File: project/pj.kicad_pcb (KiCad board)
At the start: 2 copper layers, 65 x 56.5 mm, 18 parts, among them J1 RPi_GPIO, J10 Pico PWR enable, J2 2B+, J3 zero, J4 3A+, J5 3B+, J6 4, J7 Conn_01x02, J8 Conn_01x02, J9 External PWR, SW1 SW_Push, SW2 SW_Push

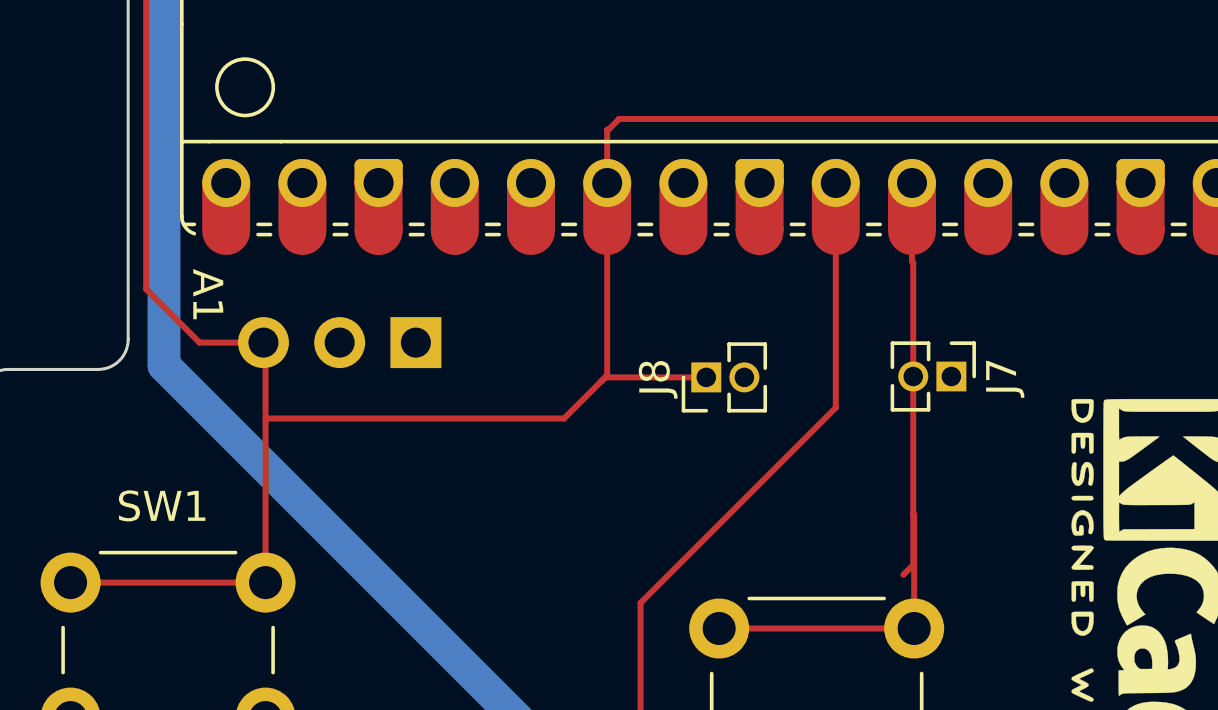
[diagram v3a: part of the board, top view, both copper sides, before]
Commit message: move holes to make room for more holes
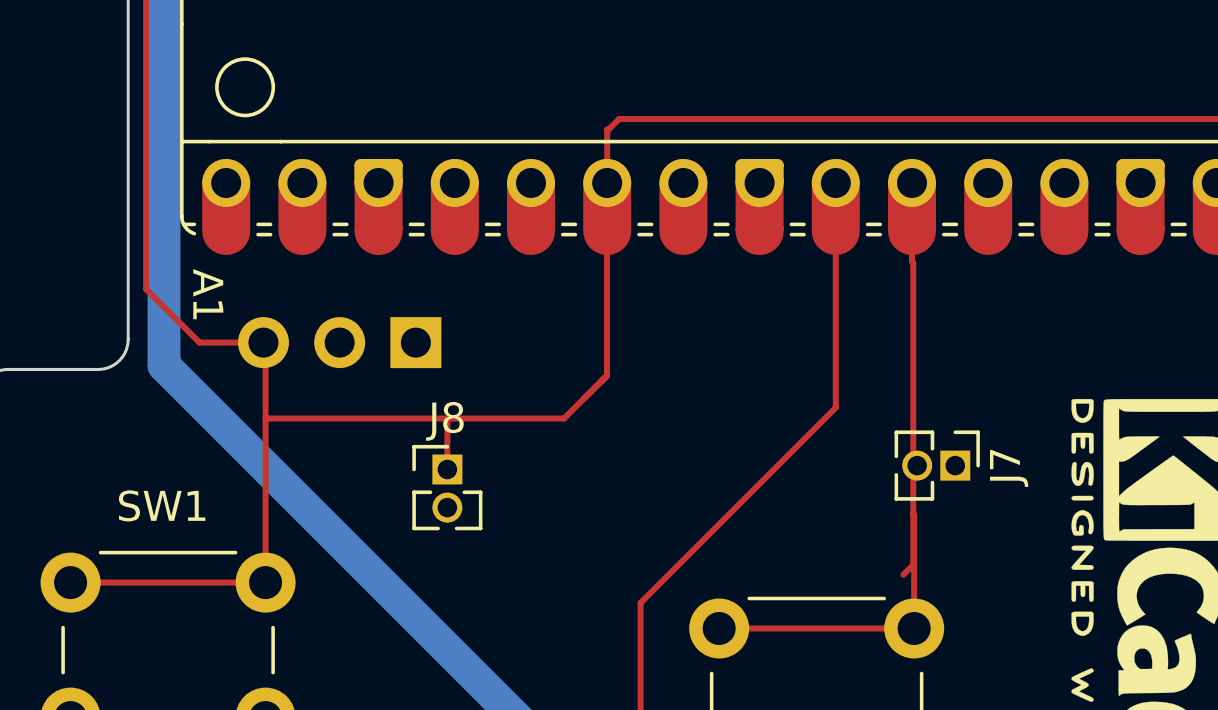
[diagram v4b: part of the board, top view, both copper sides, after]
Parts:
- moved J8 9.16 mm to (52.1, 80.8), turned to 0 degrees
- moved J7 2.97 mm to (69.0, 80.7)
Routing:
- net Net-(A1-GPIO20): track 136.3 -> 135.7 mm
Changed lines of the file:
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@@
 	(footprint "Connector_PinHeader_1.27mm:PinHeader_1x02_P1.27mm_Vertical"
 		(layer "F.Cu")
-		(at 60.69 77.76 90)
+		(at 52.06 80.83)
 		(descr "Through hole straight pin header, 1x02, 1.27mm pitch, single row")
 		(tags "Through hole pin header THT 1x02 1.27mm single row")
 		(property "Reference" "J8"
-			(at 0 -1.695 90)
+			(at 0 -1.695 360)
 			(layer "F.SilkS")
 			(effects
@@
 		)
 		(property "Value" "Conn_01x02"
-			(at 0 2.965 90)
+			(at 0 2.965 360)
 			(layer "F.Fab")
 			(effects
@@
 		)
 		(property "Footprint" "Connector_PinHeader_1.27mm:PinHeader_1x02_P1.27mm_Vertical"
-			(at 0 0 90)
+			(at 0 0 0)
 			(unlocked yes)
 			(layer "F.Fab")
@@
 		)
 		(property "Datasheet" ""
-			(at 0 0 90)
+			(at 0 0 0)
 			(unlocked yes)
 			(layer "F.Fab")
@@
 		)
 		(property "Description" "Generic connector, single row, 01x02, script generated (kicad-library-utils/schlib/autogen/connector/)"
-			(at 0 0 90)
+			(at 0 0 0)
 			(unlocked yes)
 			(layer "F.Fab")
@@
 		)
 		(fp_line
-			(start 1.11 0.76)
-			(end 1.11 1.965)
+			(start -1.11 0.76)
+			(end -1.11 1.965)
 			(stroke
 				(width 0.12)
@@
 		)
 		(fp_line
-			(start 0.563471 0.76)
-			(end 1.11 0.76)
+			(start -1.11 0.76)
+			(end -0.563471 0.76)
 			(stroke
 				(width 0.12)
@@
 		)
 		(fp_line
-			(start -1.11 0.76)
-			(end -0.563471 0.76)
+			(start -1.11 1.965)
+			(end -0.30753 1.965)
 			(stroke
 				(width 0.12)
@@
 		)
 		(fp_line
-			(start -1.11 0.76)
-			(end -1.11 1.965)
+			(start 0.30753 1.965)
+			(end 1.11 1.965)
 			(stroke
 				(width 0.12)
@@
 		)
 		(fp_line
-			(start 0.30753 1.965)
-			(end 1.11 1.965)
+			(start 0.563471 0.76)
+			(end 1.11 0.76)
 			(stroke
 				(width 0.12)
@@
 		)
 		(fp_line
-			(start -1.11 1.965)
-			(end -0.30753 1.965)
+			(start 1.11 0.76)
+			(end 1.11 1.965)
 			(stroke
 				(width 0.12)
@@
 		)
 		(fp_line
-			(start 1.55 -1.15)
-			(end -1.55 -1.15)
+			(start -1.55 -1.15)
+			(end -1.55 2.45)
 			(stroke
 				(width 0.05)
@@
 		)
 		(fp_line
-			(start -1.55 -1.15)
-			(end -1.55 2.45)
+			(start -1.55 2.45)
+			(end 1.55 2.45)
 			(stroke
 				(width 0.05)
@@
 		)
 		(fp_line
-			(start 1.55 2.45)
-			(end 1.55 -1.15)
+			(start 1.55 -1.15)
+			(end -1.55 -1.15)
 			(stroke
 				(width 0.05)
@@
 		)
 		(fp_line
-			(start -1.55 2.45)
-			(end 1.55 2.45)
+			(start 1.55 2.45)
+			(end 1.55 -1.15)
 			(stroke
 				(width 0.05)
@@
 		)
 		(fp_line
-			(start 1.05 -0.635)
-			(end 1.05 1.905)
+			(start -1.05 -0.11)
+			(end -0.525 -0.635)
 			(stroke
 				(width 0.1)
@@
 		)
 		(fp_line
-			(start -0.525 -0.635)
-			(end 1.05 -0.635)
+			(start -1.05 1.905)
+			(end -1.05 -0.11)
 			(stroke
 				(width 0.1)
@@
 		)
 		(fp_line
-			(start -1.05 -0.11)
-			(end -0.525 -0.635)
+			(start -0.525 -0.635)
+			(end 1.05 -0.635)
 			(stroke
 				(width 0.1)
@@
 		)
 		(fp_line
-			(start 1.05 1.905)
-			(end -1.05 1.905)
+			(start 1.05 -0.635)
+			(end 1.05 1.905)
 			(stroke
 				(width 0.1)
@@
 		)
 		(fp_line
-			(start -1.05 1.905)
-			(end -1.05 -0.11)
+			(start 1.05 1.905)
+			(end -1.05 1.905)
 			(stroke
 				(width 0.1)
@@
 		)
 		(fp_text user "${REFERENCE}"
-			(at 0 0.635 0)
+			(at 0 0.635 90)
 			(layer "F.Fab")
 			(effects
@@
 		)
 		(pad "1" thru_hole rect
-			(at 0 0 90)
+			(at 0 0)
 			(size 1 1)
 			(drill 0.65)
@@
 		)
 		(pad "2" thru_hole oval
-			(at 0 1.27 90)
+			(at 0 1.27)
 			(size 1 1)
 			(drill 0.65)
@@
 		(fp_arc
 			(start 10.579676 25.189937)
-			(mid 10.35796 25.493961)
+			(mid 10.357949 25.493953)
 			(end 10 25.61)
 			(stroke
@@
 	(footprint "Connector_PinHeader_1.27mm:PinHeader_1x02_P1.27mm_Vertical"
 		(layer "F.Cu")
-		(at 68.86 77.73 -90)
+		(at 68.99 80.7 -90)
 		(descr "Through hole straight pin header, 1x02, 1.27mm pitch, single row")
 		(tags "Through hole pin header THT 1x02 1.27mm single row")
@@
 	)
 	(segment
+		(start 55.95 79.13)
+		(end 56.615 78.465)
+		(width 0.2)
+		(layer "F.Cu")
+		(net 9)
+	)
+	(segment
 		(start 44.82 48.37)
 		(end 40.61 48.37)
@@
 	)
 	(segment
-		(start 60.69 77.76)
-		(end 57.32 77.76)
+		(start 57.38 76.58)
+		(end 57.38 77.7)
 		(width 0.2)
 		(layer "F.Cu")
@@
 	)
 	(segment
-		(start 57.3875 71.28)
-		(end 57.3875 77.6925)
+		(start 46 78.91)
+		(end 46 76.67)
 		(width 0.2)
 		(layer "F.Cu")
@@
 	)
 	(segment
-		(start 46 78.91)
-		(end 46 76.67)
+		(start 52.11 79.13)
+		(end 55.95 79.13)
 		(width 0.2)
 		(layer "F.Cu")
@@
 	)
 	(segment
+		(start 46 79.13)
+		(end 52.11 79.13)
+		(width 0.2)
+		(layer "F.Cu")
+		(net 9)
+	)
+	(segment
 		(start 41.28 55.91)
 		(end 41.28 59.21)
@@
 	)
 	(segment
+		(start 57.38 76.58)
+		(end 57.38 71.2875)
+		(width 0.2)
+		(layer "F.Cu")
+		(net 9)
+	)
+	(segment
 		(start 99.22 54.66)
 		(end 99.22 57.09)
@@
 	)
 	(segment
-		(start 46 79.13)
-		(end 55.95 79.13)
-		(width 0.2)
-		(layer "F.Cu")
-		(net 9)
-	)
-	(segment
 		(start 46 84.6)
 		(end 46 79.02)
@@
 	)
 	(segment
-		(start 55.95 79.13)
+		(start 56.615 78.465)
 		(end 57.18 77.9)
 		(width 0.2)
@@
 	)
 	(segment
+		(start 52.06 79.18)
+		(end 52.11 79.13)
+		(width 0.2)
+		(layer "F.Cu")
+		(net 9)
+	)
+	(segment
 		(start 39.92 52.95)
 		(end 41.23 54.26)
@@
 	)
 	(segment
+		(start 57.38 71.2875)
+		(end 57.3875 71.28)
+		(width 0.2)
+		(layer "F.Cu")
+		(net 9)
+	)
+	(segment
+		(start 57.38 77.7)
+		(end 56.615 78.465)
+		(width 0.2)
+		(layer "F.Cu")
+		(net 9)
+	)
+	(segment
 		(start 57.430056 69.5)
 		(end 57.783778 69.146278)
@@
 	)
 	(segment
+		(start 52.06 80.83)
+		(end 52.06 79.18)
+		(width 0.2)
+		(layer "F.Cu")
+		(net 9)
+	)
+	(segment
 		(start 54.8475 53.5)
 		(end 54.8475 50.0675)
@@
 	)
 	(segment
+		(start 67.5475 73.8925)
+		(end 67.59 73.935)
+		(width 0.2)
+		(layer "F.Cu")
+		(net 53)
+	)
+	(segment
 		(start 67.59 84.01)
 		(end 67.26 84.34)
@@
 	)
 	(segment
-		(start 67.59 73.935)
-		(end 67.59 77.73)
+		(start 67.5475 71.28)
+		(end 67.5475 73.8925)
 		(width 0.2)
 		(layer "F.Cu")
@@
 	)
 	(segment
-		(start 67.5475 73.8925)
-		(end 67.59 73.935)
+		(start 67.72 80.7)
+		(end 67.59 80.83)
 		(width 0.2)
 		(layer "F.Cu")
@@
 	)
 	(segment
+		(start 67.59 73.935)
+		(end 67.59 80.57)
+		(width 0.2)
+		(layer "F.Cu")
+		(net 53)
+	)
+	(segment
 		(start 67.59 82.31)
 		(end 67.59 84.01)
@@
 	)
 	(segment
-		(start 67.59 77.73)
-		(end 67.59 82.31)
+		(start 67.59 80.57)
+		(end 67.72 80.7)
 		(width 0.2)
 		(layer "F.Cu")
@@
 	)
 	(segment
-		(start 67.5475 71.28)
-		(end 67.5475 73.8925)
+		(start 67.59 80.83)
+		(end 67.59 82.31)
 		(width 0.2)
 		(layer "F.Cu")

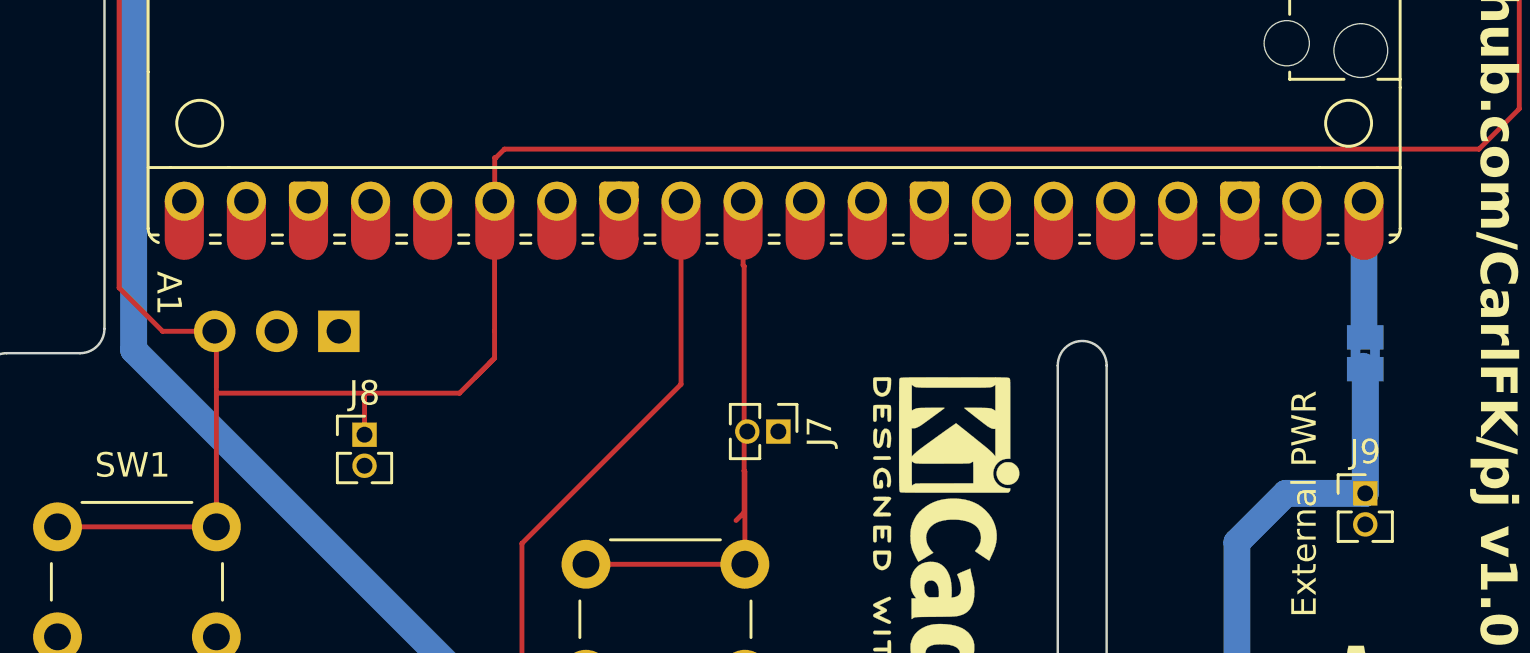
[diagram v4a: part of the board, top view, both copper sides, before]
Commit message: move reset over one, move reset headert to make room for row of holes.
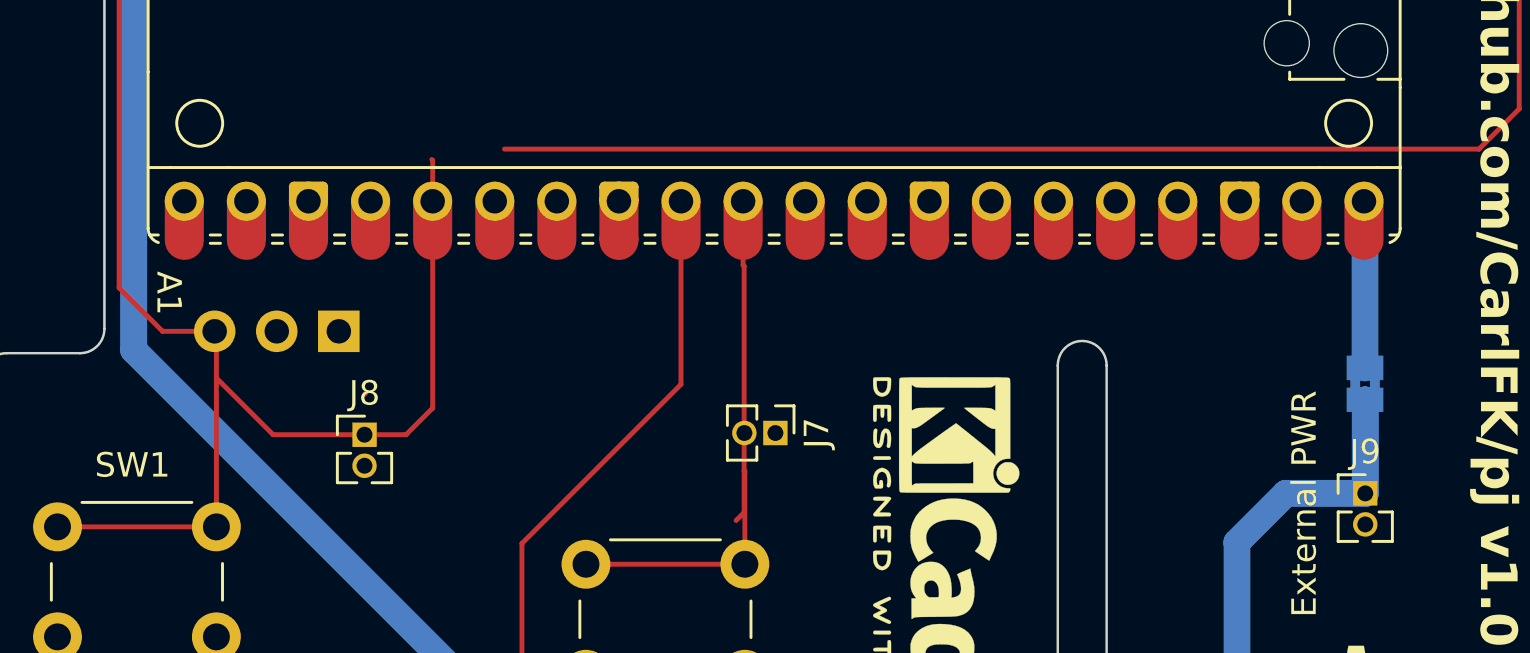
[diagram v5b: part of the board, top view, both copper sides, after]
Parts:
- moved J10 1.25 mm to (93.0, 78.8)
- moved J7 0.13 mm to (68.9, 80.8)
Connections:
- A1 pad 25: unconnected-(A1-GPIO19-Pad25) -> Net-(A1-GPIO19)
- A1 pad 26: Net-(A1-GPIO20) -> unconnected-(A1-GPIO20-Pad26)
- J2 pad 1: Net-(A1-GPIO20) -> Net-(A1-GPIO19)
- J3 pad 1: Net-(A1-GPIO20) -> Net-(A1-GPIO19)
- J5 pad 2: Net-(A1-GPIO20) -> Net-(A1-GPIO19)
- J6 pad 3: Net-(A1-GPIO20) -> Net-(A1-GPIO19)
- J8 pad 1: Net-(A1-GPIO20) -> Net-(A1-GPIO19)
- SW1 pad 1: Net-(A1-GPIO20) -> Net-(A1-GPIO19)
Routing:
- net Net-(A1-GPIO20): track 135.7 -> 0.00 mm
- net Net-(A1-GPIO19): track 0.00 -> 71.4 mm
- net unconnected-(J4-Pin_1-Pad1): track 0.00 -> 61.1 mm
- net Net-(J10-Pin_2): track 112.3 -> 110.9 mm
- net Net-(A1-VBUS): track 5.53 -> 6.91 mm

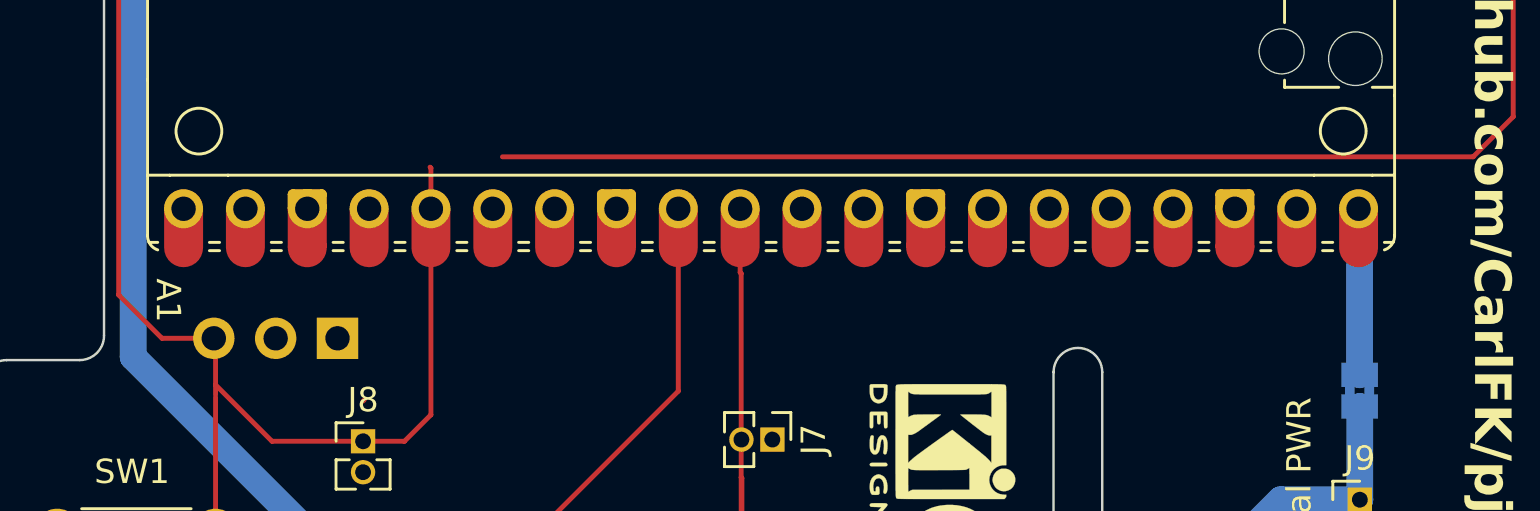
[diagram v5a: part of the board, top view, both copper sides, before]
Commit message: add 16 holes to put things in later.
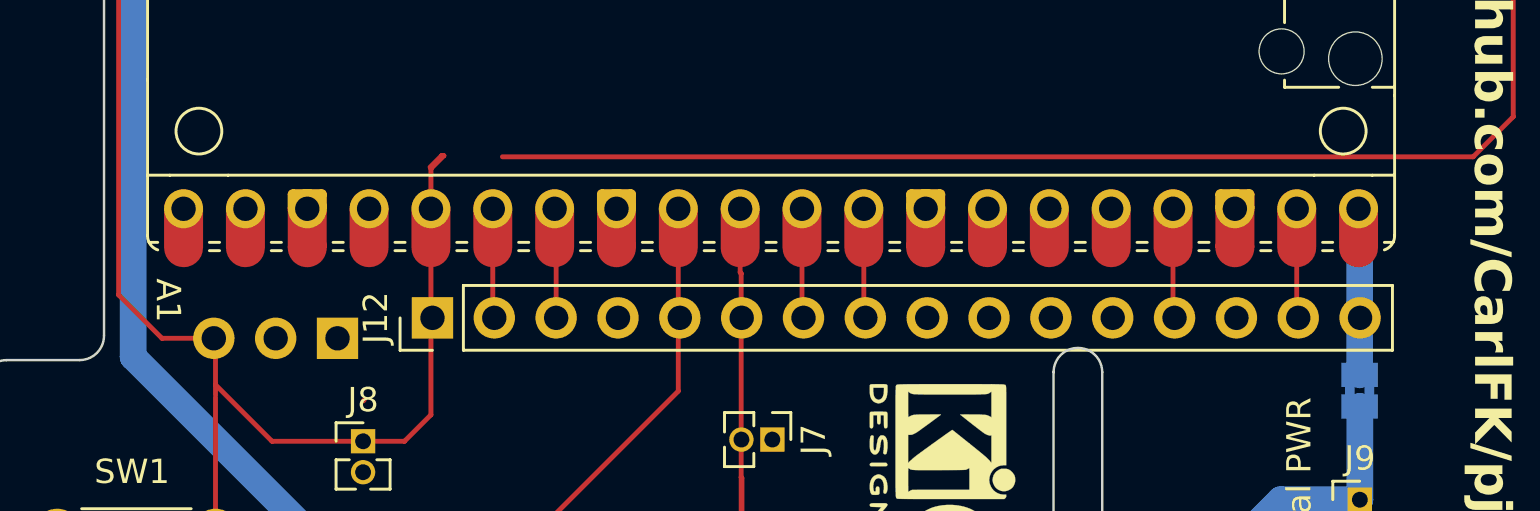
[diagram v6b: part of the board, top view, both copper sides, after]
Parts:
- added J12: Conn_01x16_Pin, Connector_PinHeader_2.54mm:PinHeader_1x16_P2.54mm_Vertical, F.Cu at (54.9, 75.8)
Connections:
- A1 pad 2: unconnected-(A1-GPIO1-Pad2) -> Net-(A1-GPIO1)
- A1 pad 26: unconnected-(A1-GPIO20-Pad26) -> Net-(A1-GPIO20)
- A1 pad 27: unconnected-(A1-GPIO21-Pad27) -> Net-(A1-GPIO21)
- A1 pad 31: unconnected-(A1-GPIO26_ADC0-Pad31) -> Net-(A1-GPIO26_ADC0)
- A1 pad 32: unconnected-(A1-GPIO27_ADC1-Pad32) -> Net-(A1-GPIO27_ADC1)
- A1 pad 33: unconnected-(A1-AGND-Pad33) -> Net-(A1-AGND)
- A1 pad 34: unconnected-(A1-GPIO28_ADC2-Pad34) -> Net-(A1-GPIO28_ADC2)
- A1 pad 35: unconnected-(A1-ADC_VREF-Pad35) -> Net-(A1-ADC_VREF)
- A1 pad 36: unconnected-(A1-3V3-Pad36) -> Net-(A1-3V3)
- A1 pad 37: unconnected-(A1-3V3_EN-Pad37) -> Net-(A1-3V3_EN)
- A1 pad 39: unconnected-(A1-VSYS-Pad39) -> Net-(A1-VSYS)
- J1 pad 8: unconnected-(J1-BCM14_TXD-Pad8) -> Net-(A1-GPIO1)
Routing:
- net Net-(A1-GPIO1): track 0.00 -> 45.8 mm
- net (no net): track 45.8 -> 0.00 mm
- net Net-(A1-GPIO20): track 0.00 -> 4.52 mm
- net Net-(A1-VSYS): track 0.00 -> 4.51 mm
- net Net-(A1-GPIO27_ADC1): track 0.00 -> 4.51 mm
- net Net-(A1-GPIO26_ADC0): track 0.00 -> 4.51 mm
- net Net-(A1-GPIO21): track 0.00 -> 4.51 mm
- net Net-(A1-3V3_EN): track 0.00 -> 4.51 mm
- net Net-(A1-GPIO19): track 71.4 -> 72.8 mm
